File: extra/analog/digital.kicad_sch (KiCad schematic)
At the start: 8 parts, among them U11 MB85RC1MT, U6 ADS1219

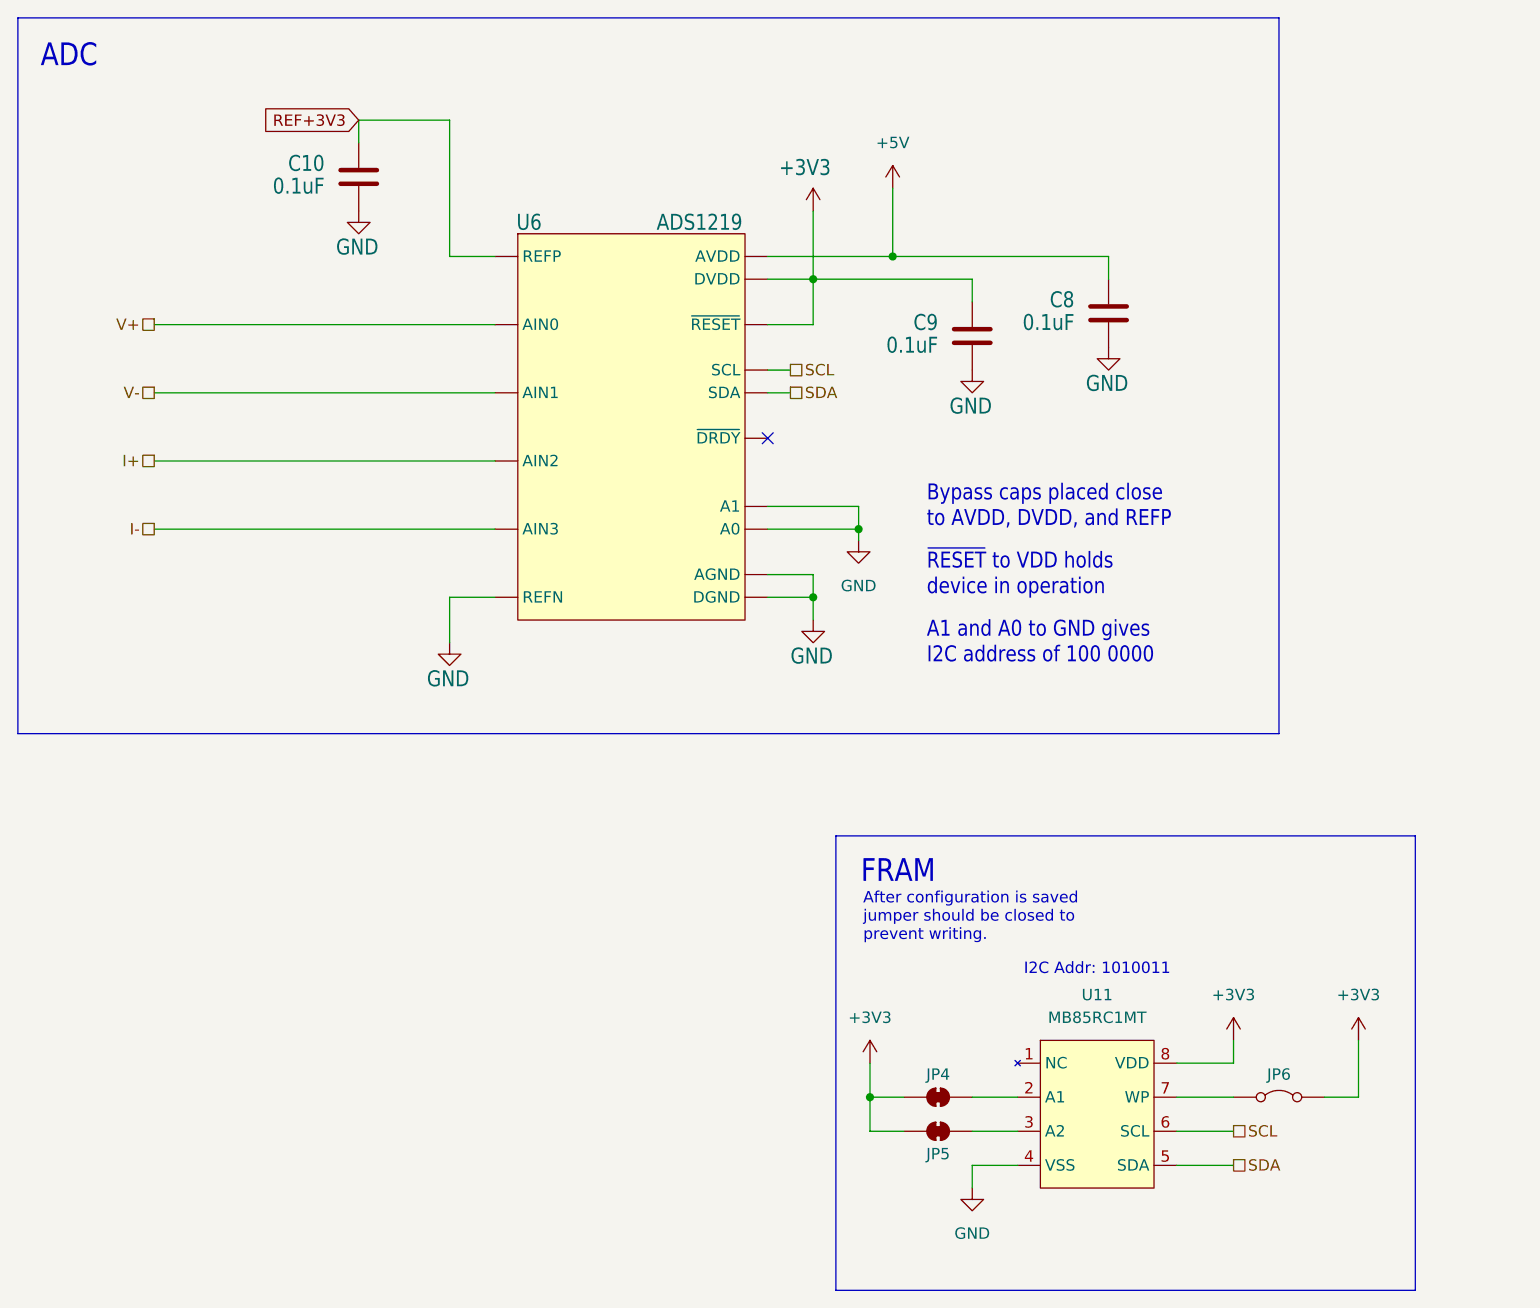
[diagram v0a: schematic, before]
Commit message: Added component values
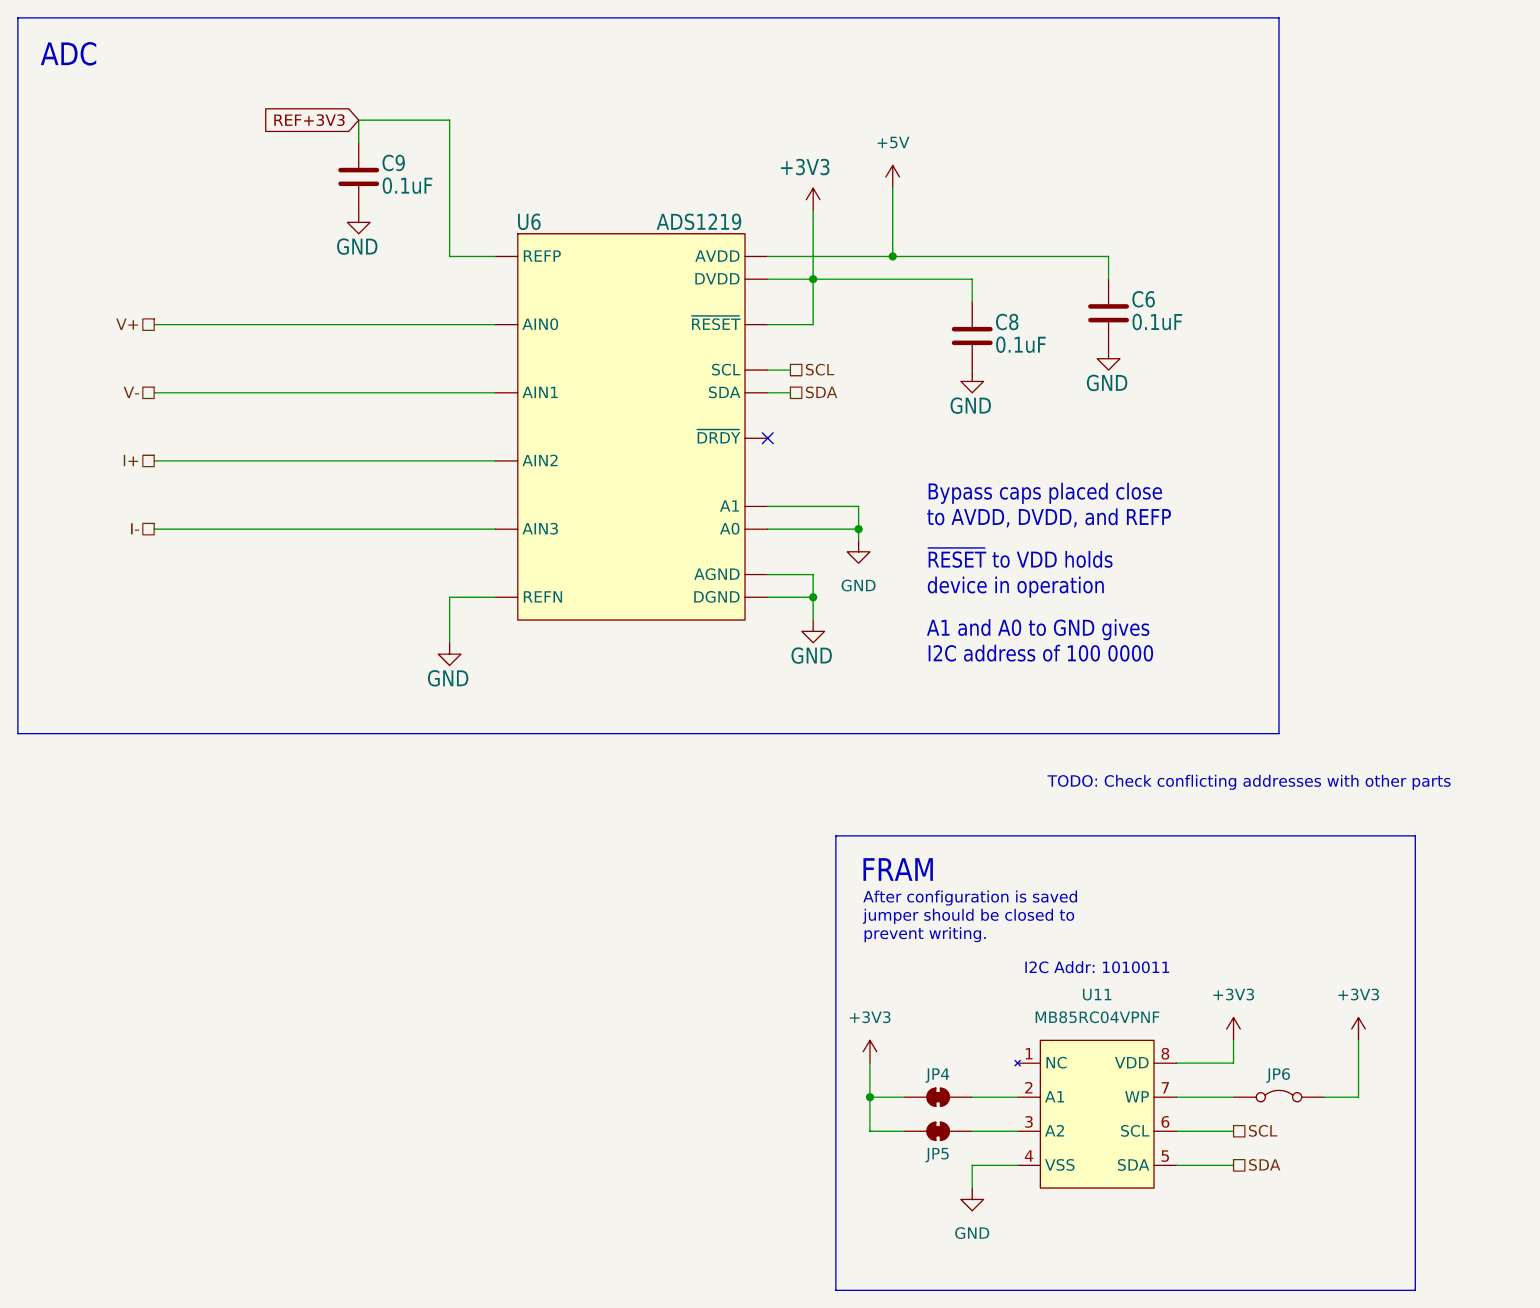
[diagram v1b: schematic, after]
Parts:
- removed C10: 0.1uF, Capacitor_SMD:C_0603_1608Metric, symbol Device:C
- added C6: 0.1uF, Capacitor_SMD:C_0603_1608Metric, symbol Device:C
- C8, C9: LCSC (none) -> C14663
- JP4, JP5: footprint (none) -> Jumper:SolderJumper-2_P1.3mm_Open_TrianglePad1.0x1.5mm; now in the parts list
- JP6: footprint (none) -> Connector_PinHeader_1.00mm:PinHeader_1x02_P1.00mm_Vertical
- U11: value MB85RC1MT -> MB85RC04VPNF; footprint Soil Power Sensor:SOP127P505X155-8N -> Package_SO:SSOP-8_3.9x5.05mm_P1.27mm; LCSC (none) -> C8738
- U6: footprint Soil Power Sensor:TSSOP65P640X120-16 -> Package_SO:TSSOP-16_4.4x5mm_P0.65mm; LCSC (none) -> C2869313
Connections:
- net +3V3: now also C8.1; no longer C9.1
- net +5V: now also C6.1; no longer C8.1
- net GND: now also C6.2
- net REF+3V3: now also C9.1
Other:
- note added: "TODO: Check conflicting addresses with other parts"

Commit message: Placed and routed components
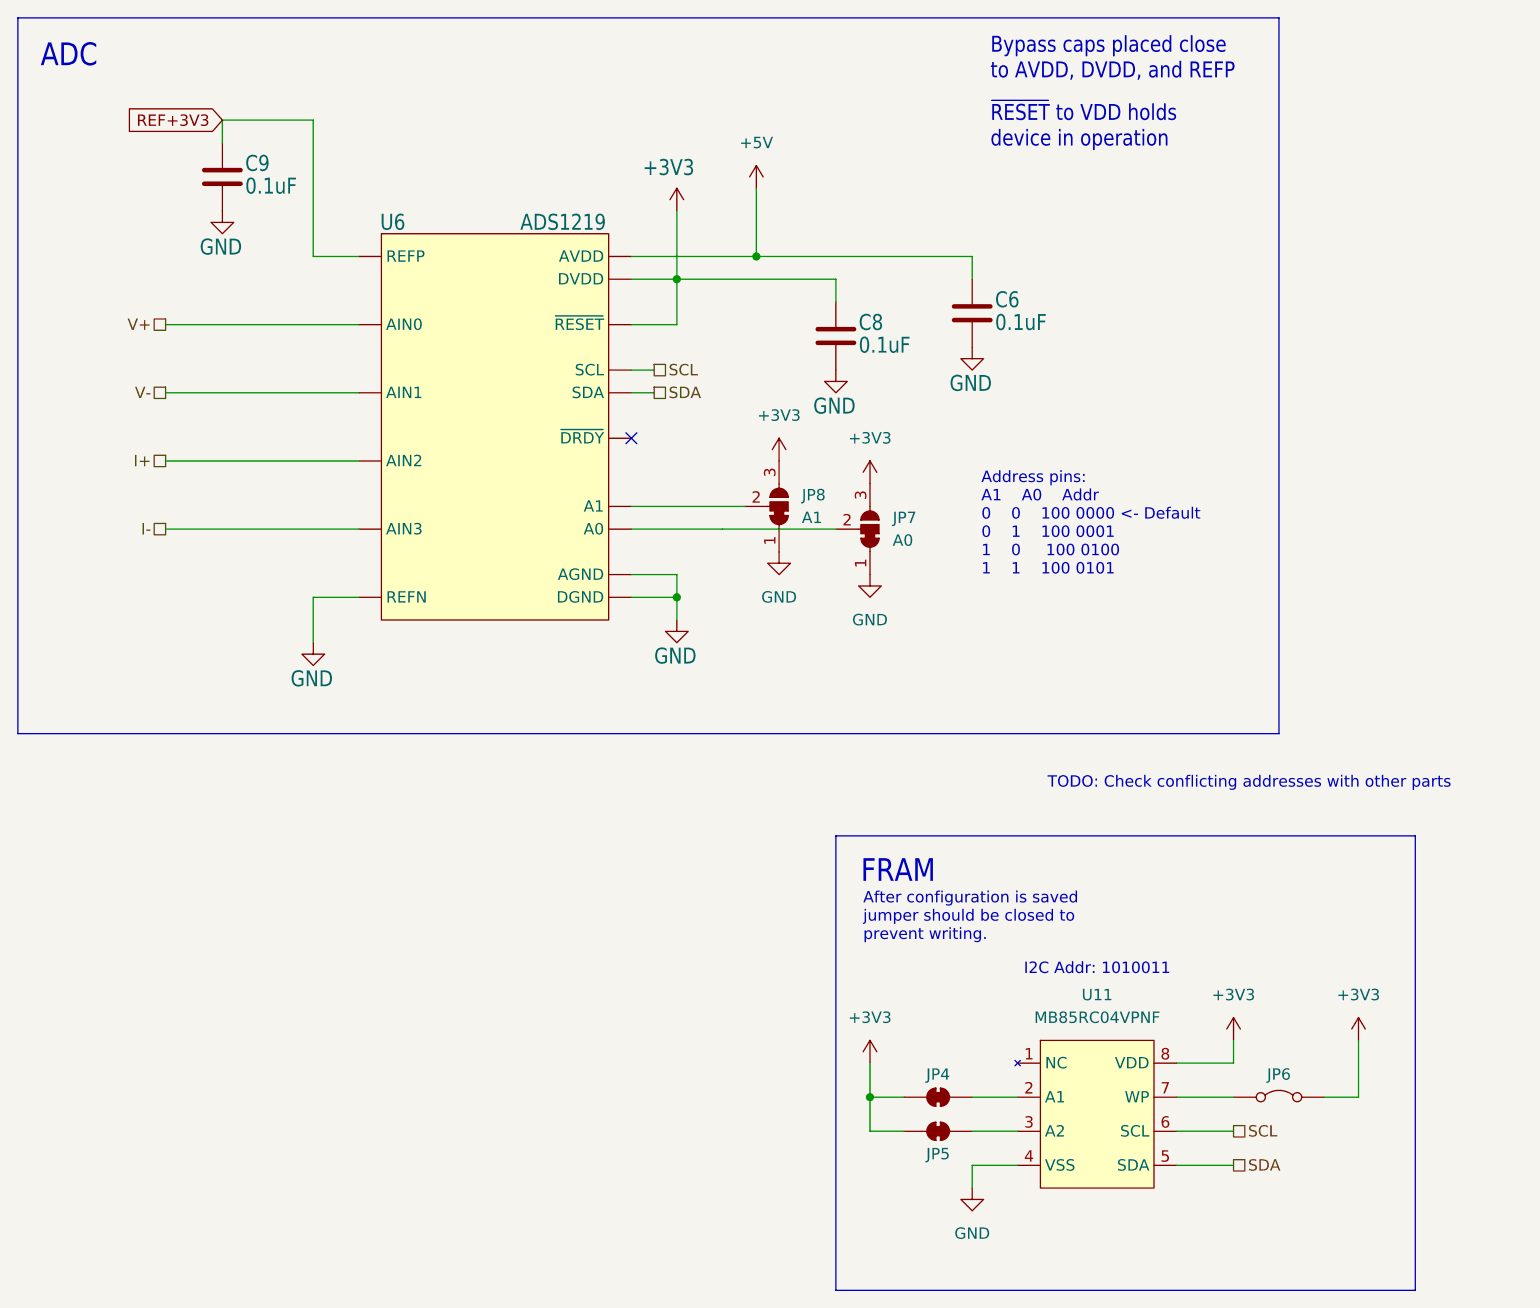
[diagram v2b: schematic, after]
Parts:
- added JP7: A0, Jumper:SolderJumper-3_P1.3mm_Bridged12_Pad1.0x1.5mm, symbol Jumper:SolderJumper_3_Bridged12
- added JP8: A1, Jumper:SolderJumper-3_P1.3mm_Bridged12_Pad1.0x1.5mm, symbol Jumper:SolderJumper_3_Bridged12
- JP6: footprint Connector_PinHeader_1.00mm:PinHeader_1x02_P1.00mm_Vertical -> Connector_PinHeader_2.54mm:PinHeader_1x02_P2.54mm_Vertical
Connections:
- net +3V3: now also U6.13 (DVDD), U6.3 (~{RESET}), JP7.3 (B), JP8.3 (B); no longer U6.PIN13 (DVDD), U6.PIN3 (~{RESET})
- net +5V: now also U6.12 (AVDD); no longer U6.PIN12 (AVDD)
- net GND: now also U6.4 (DGND), U6.5 (AGND), U6.8 (REFN), JP7.1 (A), JP8.1 (A); no longer U6.PIN1 (A0), U6.PIN2 (A1), U6.PIN4 (DGND), U6.PIN5 (AGND), U6.PIN8 (REFN)
- net I+: now also U6.7 (AIN2); no longer U6.PIN7 (AIN2)
- net I-: now also U6.6 (AIN3); no longer U6.PIN6 (AIN3)
- net REF+3V3: now also U6.9 (REFP); no longer U6.PIN9 (REFP)
- net SCL: now also U6.16 (SCL); no longer U6.PIN16 (SCL)
- net SDA: now also U6.15 (SDA); no longer U6.PIN15 (SDA)
- net V+: now also U6.11 (AIN0); no longer U6.PIN11 (AIN0)
- net V-: now also U6.10 (AIN1); no longer U6.PIN10 (AIN1)
- new net: JP7.2 (C), U6.1 (A0)
- new net: JP8.2 (C), U6.2 (A1)
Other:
- note added: "Address pins: A1 A0 Addr 0 0 100 0000 <- Default 0 1 100 0001 1 0 100 0100 1 1 100 0101"
- note removed: "A1 and A0 to GND gives I2C address of 100 0000"
- moved on the sheet: C6, C8, C9, U6

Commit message: Finalization with jack
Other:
- company: (none) -> jlab
- title: (none) -> Analog Frontend
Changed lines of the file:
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@@
 	(generator_version "9.0")
 	(paper "A4")
+	(title_block
+		(title "Analog Frontend")
+		(date "2026-03-13")
+		(rev "v3.0.0")
+		(company "jlab")
+	)
 	(rectangle
 		(start 113.03 16.51)

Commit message: Hardware fixes
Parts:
- JP4, JP5: footprint Jumper:SolderJumper-2_P1.3mm_Open_TrianglePad1.0x1.5mm -> Jumper:SolderJumper-2_P1.3mm_Open_RoundedPad1.0x1.5mm
- JP7, JP8: footprint Jumper:SolderJumper-3_P1.3mm_Bridged12_Pad1.0x1.5mm -> Jumper:SolderJumper-3_P1.3mm_Open_RoundedPad1.0x1.5mm
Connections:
- net +5V renamed +4.6V
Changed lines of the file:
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@@
 			)
 		)
-		(property "Footprint" "Jumper:SolderJumper-3_P1.3mm_Bridged12_Pad1.0x1.5mm"
+		(property "Footprint" "Jumper:SolderJumper-3_P1.3mm_Open_RoundedPad1.0x1.5mm"
 			(at 208.28 73.66 0)
 			(effects
@@
 			)
 		)
-		(property "Footprint" "Jumper:SolderJumper-2_P1.3mm_Open_TrianglePad1.0x1.5mm"
+		(property "Footprint" "Jumper:SolderJumper-2_P1.3mm_Open_RoundedPad1.0x1.5mm"
 			(at 215.9 137.16 0)
 			(effects
@@
 			)
 		)
-		(property "Footprint" "Jumper:SolderJumper-2_P1.3mm_Open_TrianglePad1.0x1.5mm"
+		(property "Footprint" "Jumper:SolderJumper-2_P1.3mm_Open_RoundedPad1.0x1.5mm"
 			(at 215.9 140.97 0)
 			(effects
@@
 			)
 		)
-		(property "Footprint" "Jumper:SolderJumper-3_P1.3mm_Bridged12_Pad1.0x1.5mm"
+		(property "Footprint" "Jumper:SolderJumper-3_P1.3mm_Open_RoundedPad1.0x1.5mm"
 			(at 198.12 71.12 0)
 			(effects
@@
 		(on_board yes)
 		(dnp no)
-		(fields_autoplaced yes)
 		(property "Reference" "#PWR018"
 			(at 195.58 39.37 0)
@@
 			)
 		)
-		(property "Value" "+5V"
-			(at 195.58 30.48 0)
-			(effects
-				(font
-					(size 1.27 1.27)
-				)
-			)
-		)
+		(property "Value" "+4.6V"
+			(at 192.532 30.988 0)
+			(effects
+				(font
+					(size 1.27 1.27)
+				)
+				(justify left)
+			)
+		)

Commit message: Generated production files
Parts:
- JP6: now left out of the parts list
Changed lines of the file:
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@@
 	(title_block
 		(title "Analog Frontend")
-		(date "2026-03-13")
-		(rev "v3.0.0")
+		(date "2026-04-06")
+		(rev "v3.1.0")
 		(company "jlab")
 	)
@@
 		(unit 1)
 		(exclude_from_sim no)
-		(in_bom yes)
+		(in_bom no)
 		(on_board yes)
 		(dnp no)
